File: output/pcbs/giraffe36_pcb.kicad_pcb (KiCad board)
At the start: 2 copper layers, 137.7 x 109.4 mm, 20 parts

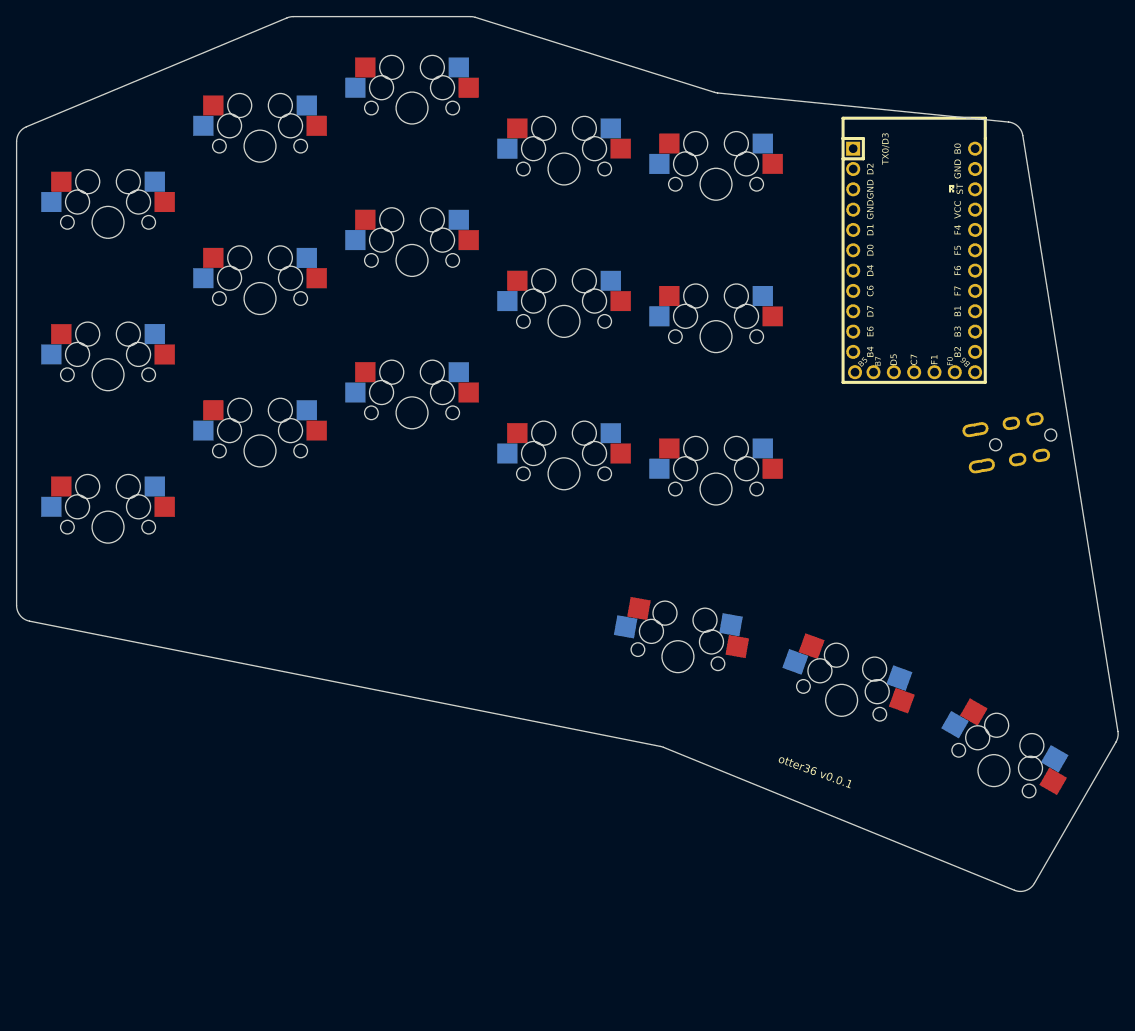
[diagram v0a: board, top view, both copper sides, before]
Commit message: rename otter -> giraffe, more thumb splay and fillet
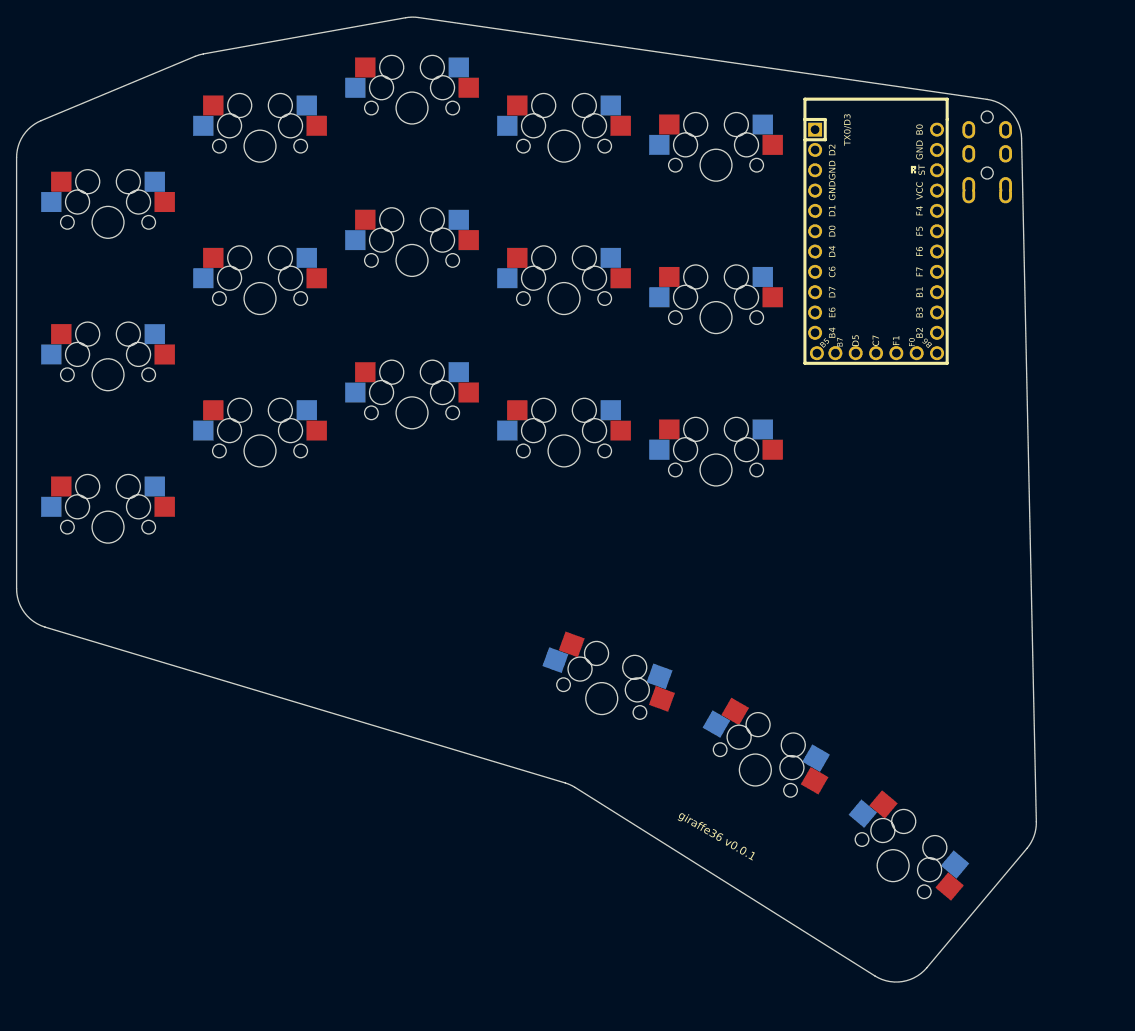
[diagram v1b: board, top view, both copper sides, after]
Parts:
- moved TRRS1 44.0 mm to (264.6, 99.5), turned to 0 degrees
- moved S18 17.3 mm to (250.5, 194.7), turned to -40 degrees
- moved S17 13.9 mm to (233.3, 182.8), turned to -30 degrees
- moved S16 10.9 mm to (214.1, 173.8), turned to -20 degrees
- moved ? 5.32 mm to (248.4, 116.7)
- moved S10 2.86 mm to (209.4, 142.9)
- moved S11 2.86 mm to (209.4, 123.8)
- moved S12 2.86 mm to (209.4, 104.8)
- moved S13 2.38 mm to (228.4, 145.3)
- moved S14 2.38 mm to (228.4, 126.2)
- moved S15 2.38 mm to (228.4, 107.2)
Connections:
- ? pad 1: (no net) -> matrix_index_top
- ? pad 10: (no net) -> matrix_middle_home
- ? pad 11: (no net) -> matrix_ring_home
- ? pad 12: (no net) -> matrix_pinky_home
- ? pad 13: (no net) -> thumbfan_near_home
- ? pad 14: (no net) -> thumbfan_home_home
- ? pad 15: (no net) -> thumbfan_far_home
- ? pad 16: (no net) -> B1
- ? pad 17: (no net) -> F7
- ? pad 18: (no net) -> F6
- ? pad 19: (no net) -> F5
- ? pad 2: (no net) -> matrix_inner_top
- ? pad 20: (no net) -> F4
- ? pad 21: (no net) -> VCC
- ? pad 22: (no net) -> RST
- ? pad 23: (no net) -> GND
- ? pad 24: (no net) -> B0
- ? pad 25: (no net) -> matrix_middle_bottom
- ? pad 26: (no net) -> matrix_index_bottom
- ? pad 27: (no net) -> matrix_inner_bottom
- ? pad 28: (no net) -> matrix_ring_bottom
- ? pad 29: (no net) -> matrix_pinky_bottom
- ? pad 3: (no net) -> GND
- ? pad 4: (no net) -> GND
- ? pad 5: (no net) -> matrix_middle_top
- ? pad 6: (no net) -> matrix_ring_top
- ? pad 7: (no net) -> matrix_pinky_top
- ? pad 8: (no net) -> matrix_index_home
- ? pad 9: (no net) -> matrix_inner_home
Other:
- board size 137.7 x 109.4 mm -> 127.5 x 120.6 mm
- board text added: "giraffe36 v0.0.1"
- board text removed: "otter36 v0.0.1"

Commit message: tweak outlines and routing
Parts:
- moved ? 0.48 mm to (248.9, 116.7)
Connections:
- ? pad 10: matrix_middle_home -> matrix_inner_home
- ? pad 8: matrix_index_home -> matrix_middle_home
- ? pad 9: matrix_inner_home -> matrix_index_home
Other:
- board size 127.5 x 120.6 mm -> 125.8 x 118.4 mm
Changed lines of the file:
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@@
         )
     (module "Elite-C" (layer "F.Cu")
-      (at 248.4025 116.68125 270)
+      (at 248.87875 116.68125 270)
       (attr through_hole)
       (fp_text value "Elite-C" (at 0 0) (layer "F.SilkS") hide
@@
       (pad "6" thru_hole circle (at -1.27 7.62) (size 1.7526 1.7526) (drill 1.0922) (layers *.Cu *.SilkS *.Mask) (net 7 "matrix_ring_top"))
       (pad "7" thru_hole circle (at 1.27 7.62) (size 1.7526 1.7526) (drill 1.0922) (layers *.Cu *.SilkS *.Mask) (net 4 "matrix_pinky_top"))
-      (pad "8" thru_hole circle (at 3.81 7.62) (size 1.7526 1.7526) (drill 1.0922) (layers *.Cu *.SilkS *.Mask) (net 12 "matrix_index_home"))
-      (pad "9" thru_hole circle (at 6.35 7.62) (size 1.7526 1.7526) (drill 1.0922) (layers *.Cu *.SilkS *.Mask) (net 15 "matrix_inner_home"))
-      (pad "10" thru_hole circle (at 8.89 7.62) (size 1.7526 1.7526) (drill 1.0922) (layers *.Cu *.SilkS *.Mask) (net 9 "matrix_middle_home"))
+      (pad "8" thru_hole circle (at 3.81 7.62) (size 1.7526 1.7526) (drill 1.0922) (layers *.Cu *.SilkS *.Mask) (net 9 "matrix_middle_home"))
+      (pad "9" thru_hole circle (at 6.35 7.62) (size 1.7526 1.7526) (drill 1.0922) (layers *.Cu *.SilkS *.Mask) (net 12 "matrix_index_home"))
+      (pad "10" thru_hole circle (at 8.89 7.62) (size 1.7526 1.7526) (drill 1.0922) (layers *.Cu *.SilkS *.Mask) (net 15 "matrix_inner_home"))
       (pad "11" thru_hole circle (at 11.43 7.62) (size 1.7526 1.7526) (drill 1.0922) (layers *.Cu *.SilkS *.Mask) (net 6 "matrix_ring_home"))
       (pad "12" thru_hole circle (at 13.97 7.3914) (size 1.7526 1.7526) (drill 1.0922) (layers *.Cu *.SilkS *.Mask) (net 3 "matrix_pinky_home"))
@@
                 (effects (font (size 1 1) (thickness 0.15)) )
             )
-            (gr_line (start 268.43787433146827 189.2364429923946) (end 266.5915397481229 103.7734355283701) (angle 90) (layer Edge.Cuts) (width 0.15))
-(gr_line (start 262.3050591786624 98.93243484859755) (end 191.1986430372401 88.69745579722957) (angle 90) (layer Edge.Cuts) (width 0.15))
-(gr_line (start 189.6057370284023 88.72459907596672) (end 164.31994965775277 93.24839931461129) (angle 90) (layer Edge.Cuts) (width 0.15))
-(gr_line (start 163.2738356048592 93.55636413256097) (end 144.04333296444227 101.58663759376094) (angle 90) (layer Edge.Cuts) (width 0.15))
-(gr_line (start 140.97 106.20052467891279) (end 140.97 160.10840398922608) (angle 90) (layer Edge.Cuts) (width 0.15))
-(gr_line (start 144.5350394450162 164.8980686727532) (end 209.55217616364516 184.37689015349645) (angle 90) (layer Edge.Cuts) (width 0.15))
-(gr_line (start 210.77856208033032 184.93367938208416) (end 248.2577161049487 208.4980418824439) (angle 90) (layer Edge.Cuts) (width 0.15))
-(gr_line (start 254.74928474322292 207.4791045673029) (end 267.2692629024389 192.55837563426132) (angle 90) (layer Edge.Cuts) (width 0.15))
-(gr_arc (start 261.5927061524883 103.88143003043842) (end 266.5915397524883 103.77343553043842) (angle -80.57154310169524) (layer Edge.Cuts) (width 0.15))
-(gr_arc (start 190.48629001106642 93.64645097906825) (end 191.19864301106642 88.69745577906825) (angle -18.334129319859528) (layer Edge.Cuts) (width 0.15))
-(gr_arc (start 165.20050264041691 98.1702512177128) (end 164.31994964041692 93.2483993177128) (angle -12.521145693837937) (layer Edge.Cuts) (width 0.15))
-(gr_arc (start 145.97 106.20052467891279) (end 144.043333 101.58663757891279) (angle -67.3355598115637) (layer Edge.Cuts) (width 0.15))
-(gr_arc (start 145.97 160.10840398922608) (end 140.97 160.10840398922608) (angle -73.32203635384576) (layer Edge.Cuts) (width 0.15))
-(gr_arc (start 208.11721560866138 189.1665548370236) (end 210.7785621086614 184.9336793370236) (angle -15.480947111767009) (layer Edge.Cuts) (width 0.15))
-(gr_arc (start 250.91906257661768 204.26516642750448) (end 248.25771607661767 208.4980419275045) (angle -82.1589095950444) (layer Edge.Cuts) (width 0.15))
-(gr_arc (start 263.4390407358337 189.34443749446302) (end 267.2692629358337 192.55837559446303) (angle -41.23762323591903) (layer Edge.Cuts) (width 0.15))
+            (gr_line (start 267.7233337781094 188.64636047823296) (end 266.5585210459172 103.79904152942254) (angle 90) (layer Edge.Cuts) (width 0.15))
+(gr_line (start 262.28155811664254 98.92016220960969) (end 198.37937702494528 89.58748568152359) (angle 90) (layer Edge.Cuts) (width 0.15))
+(gr_line (start 197.6568110514561 89.53500000000003) (end 174.34119148542428 89.53500000000003) (angle 90) (layer Edge.Cuts) (width 0.15))
+(gr_line (start 172.26670854038835 89.98565712053627) (end 144.84801705496412 102.48847542734222) (angle 90) (layer Edge.Cuts) (width 0.15))
+(gr_line (start 141.9225 107.037818306806) (end 141.9225 159.16861772182457) (angle 90) (layer Edge.Cuts) (width 0.15))
+(gr_line (start 145.47185401934755 163.95355515800708) (end 209.89369569872298 183.48427952349323) (angle 90) (layer Edge.Cuts) (width 0.15))
+(gr_line (start 211.09200633600454 184.02857677087837) (end 248.14444404538048 207.17373776925433) (angle 90) (layer Edge.Cuts) (width 0.15))
+(gr_line (start 254.62362278067937 206.14703567893775) (end 266.5540269927103 191.92893357538117) (angle 90) (layer Edge.Cuts) (width 0.15))
+(gr_arc (start 261.5589921431532 103.86767652808703) (end 266.5585210431532 103.79904152808703) (angle -80.90438567212655) (layer Edge.Cuts) (width 0.15))
+(gr_arc (start 197.6568110514561 94.53500000000003) (end 198.3793770514561 89.58748560000002) (angle -8.309090475830658) (layer Edge.Cuts) (width 0.15))
+(gr_arc (start 174.34119148542428 94.53500000000003) (end 174.34119148542428 89.53500000000003) (angle -24.5128043054565) (layer Edge.Cuts) (width 0.15))
+(gr_arc (start 146.9225 107.037818306806) (end 144.84801710000002 102.488475406806) (angle -65.48719569454393) (layer Edge.Cuts) (width 0.15))
+(gr_arc (start 146.9225 159.16861772182457) (end 141.9225 159.16861772182457) (angle -73.1343090469096) (layer Edge.Cuts) (width 0.15))
+(gr_arc (start 208.4430497180705 188.2692169596757) (end 211.0920063180705 184.0285767596757) (angle -15.125665267156585) (layer Edge.Cuts) (width 0.15))
+(gr_arc (start 250.7934006633145 202.933097580457) (end 248.1444440633145 207.173737780457) (angle -81.99135505737092) (layer Edge.Cuts) (width 0.15))
+(gr_arc (start 262.7238048753455 188.7149954769004) (end 266.55402707534546 191.92893357690042) (angle -40.786525014952915) (layer Edge.Cuts) (width 0.15))
 )

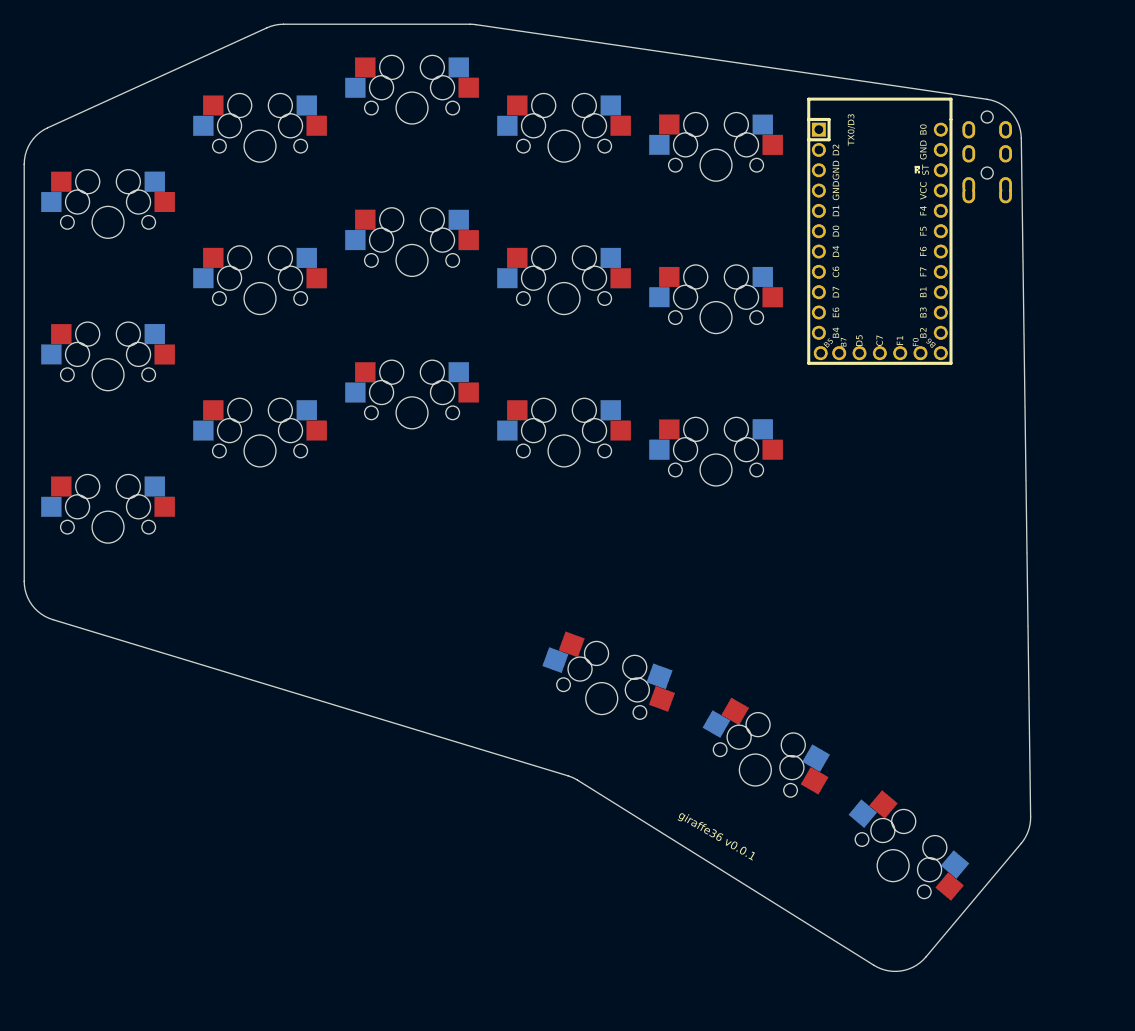
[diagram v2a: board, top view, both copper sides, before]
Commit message: reduce pinky stagger
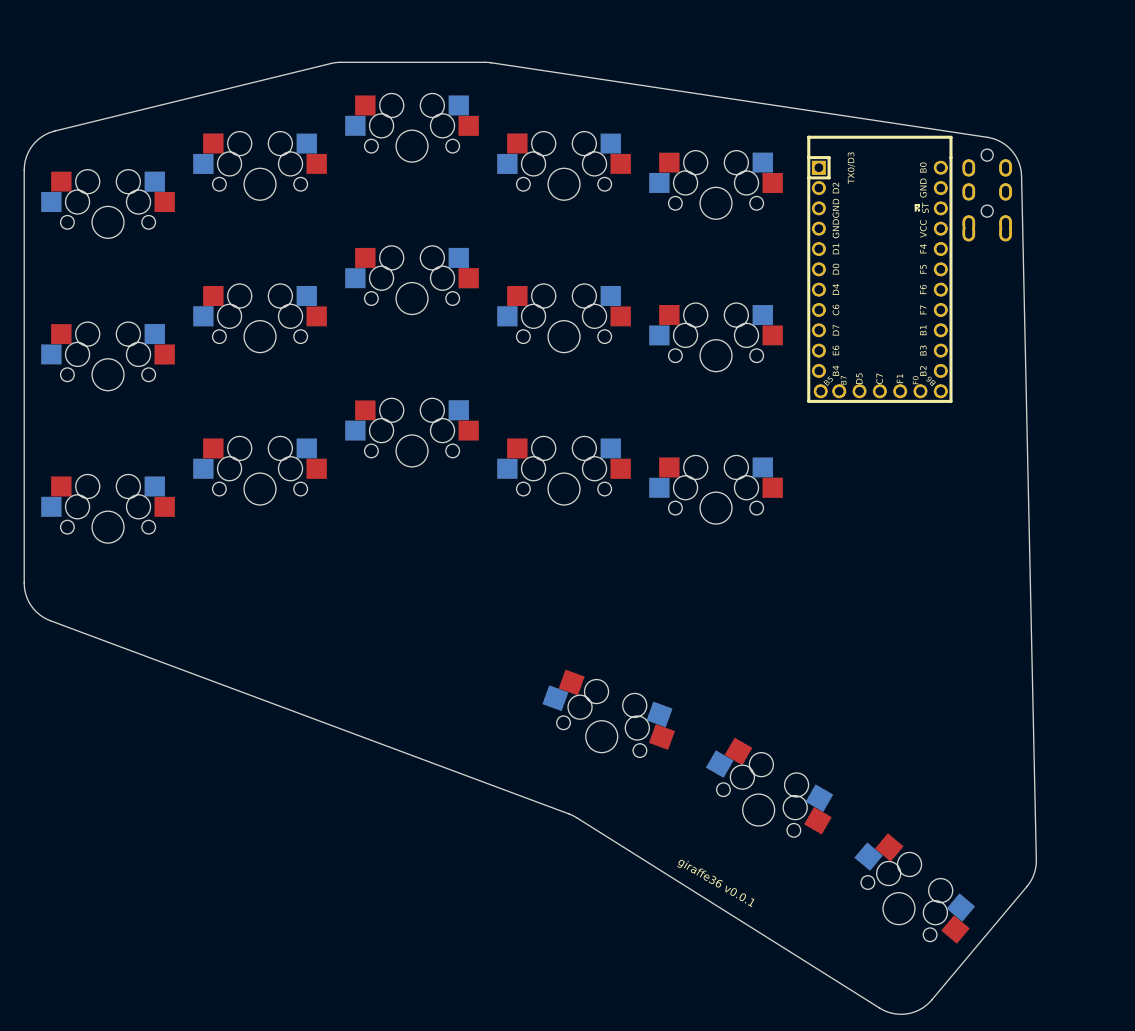
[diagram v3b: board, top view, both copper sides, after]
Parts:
- moved S18 5.42 mm to (251.3, 200.1)
- moved S17 5.02 mm to (233.7, 187.8)
- moved S10 4.76 mm to (209.4, 147.6)
- moved S13 4.76 mm to (228.4, 150.0)
- moved S16 4.76 mm to (214.1, 178.6)
- moved S4 4.76 mm to (171.4, 147.6)
- moved ? 4.76 mm to (248.9, 121.4)
- moved S11 4.76 mm to (209.4, 128.6)
- moved S12 4.76 mm to (209.4, 109.5)
- moved S14 4.76 mm to (228.4, 131.0)
- moved S15 4.76 mm to (228.4, 111.9)
- moved S5 4.76 mm to (171.4, 128.6)
- moved S6 4.76 mm to (171.4, 109.5)
- moved TRRS1 4.76 mm to (264.6, 104.3)
- moved S7 4.76 mm to (190.4, 142.9)
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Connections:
- ? pad 28: matrix_ring_bottom -> matrix_pinky_bottom
- ? pad 29: matrix_pinky_bottom -> matrix_ring_bottom
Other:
- board size 125.8 x 118.4 mm -> 126.5 x 119 mm

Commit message: remove hotswap
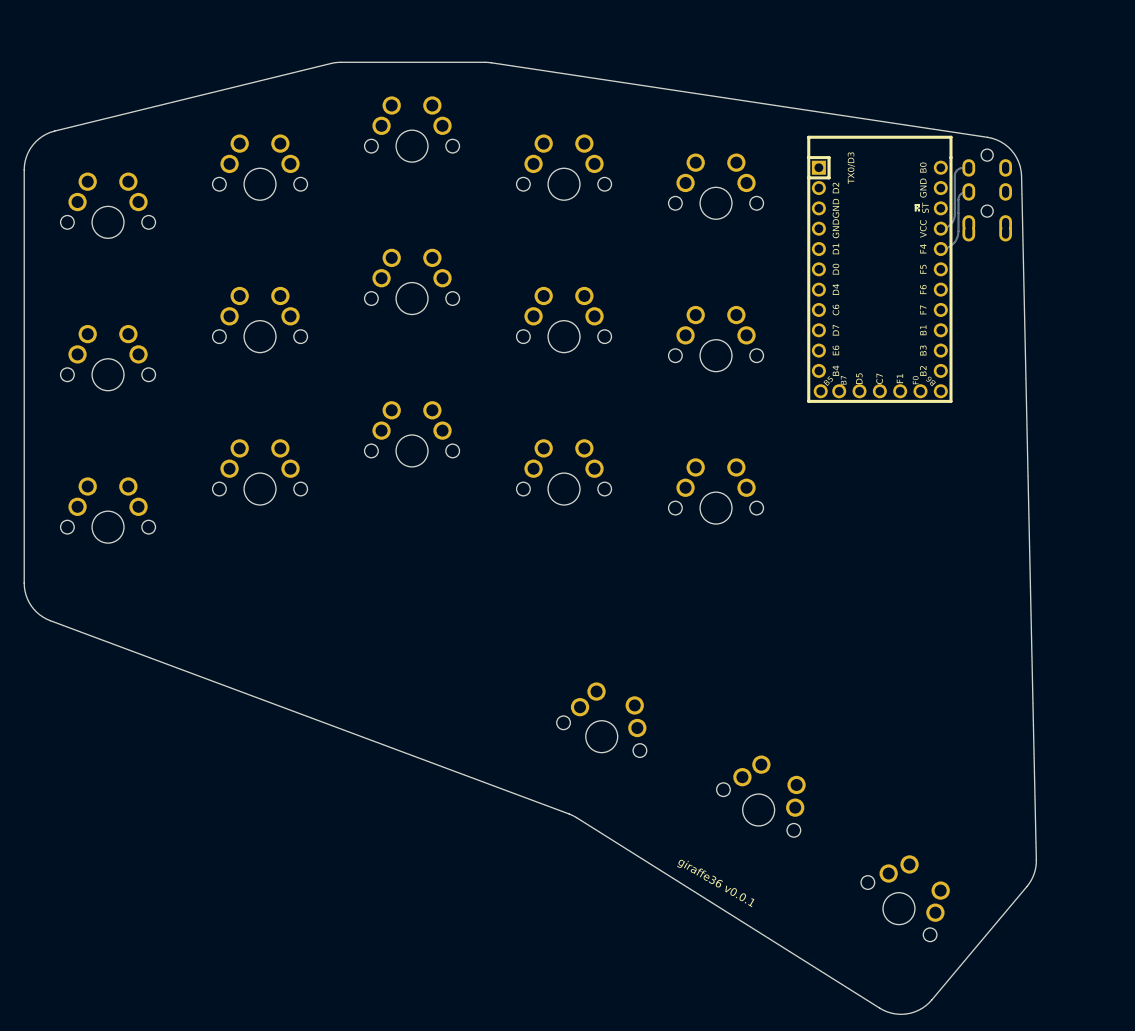
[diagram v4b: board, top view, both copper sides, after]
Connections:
- ? pad 1: matrix_index_top -> matrix_inner_top
- ? pad 2: matrix_inner_top -> matrix_index_top
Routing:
- net VCC: track 0.00 -> 9.80 mm
- net F4: track 0.00 -> 9.14 mm
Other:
- net class Default removed

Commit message: preparing for first prototypes
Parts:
- removed ?: Elite-C, Elite-C
- added U0: Pico, RPi_Pico_TH_oval_face_up, F.Cu at (249.4, 129.1)
- moved TRRS1 2.86 mm to (267.5, 104.3)
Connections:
- TRRS1 pad 1: GND -> VSYS
- TRRS1 pad 3: F4 -> GP1
- TRRS1 pad 4: VCC -> GP0
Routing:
- net VCC: track 9.80 -> 0.00 mm
- net F4: track 9.14 -> 0.00 mm
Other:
- board size 126.5 x 119 mm -> 130.1 x 119 mm
- net class Default added: clearance 0.2, trace_width 0.25, via_dia 0.8, via_drill 0.4
- board text added: "JLCJLCJLC"
